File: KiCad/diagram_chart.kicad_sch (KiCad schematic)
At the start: 35 parts, among them J1 Barrel_Jack_Switch_Pin3Ring, J2 Screw_Terminal_01x02, SW0 SW_SPDT, U2 74HC165

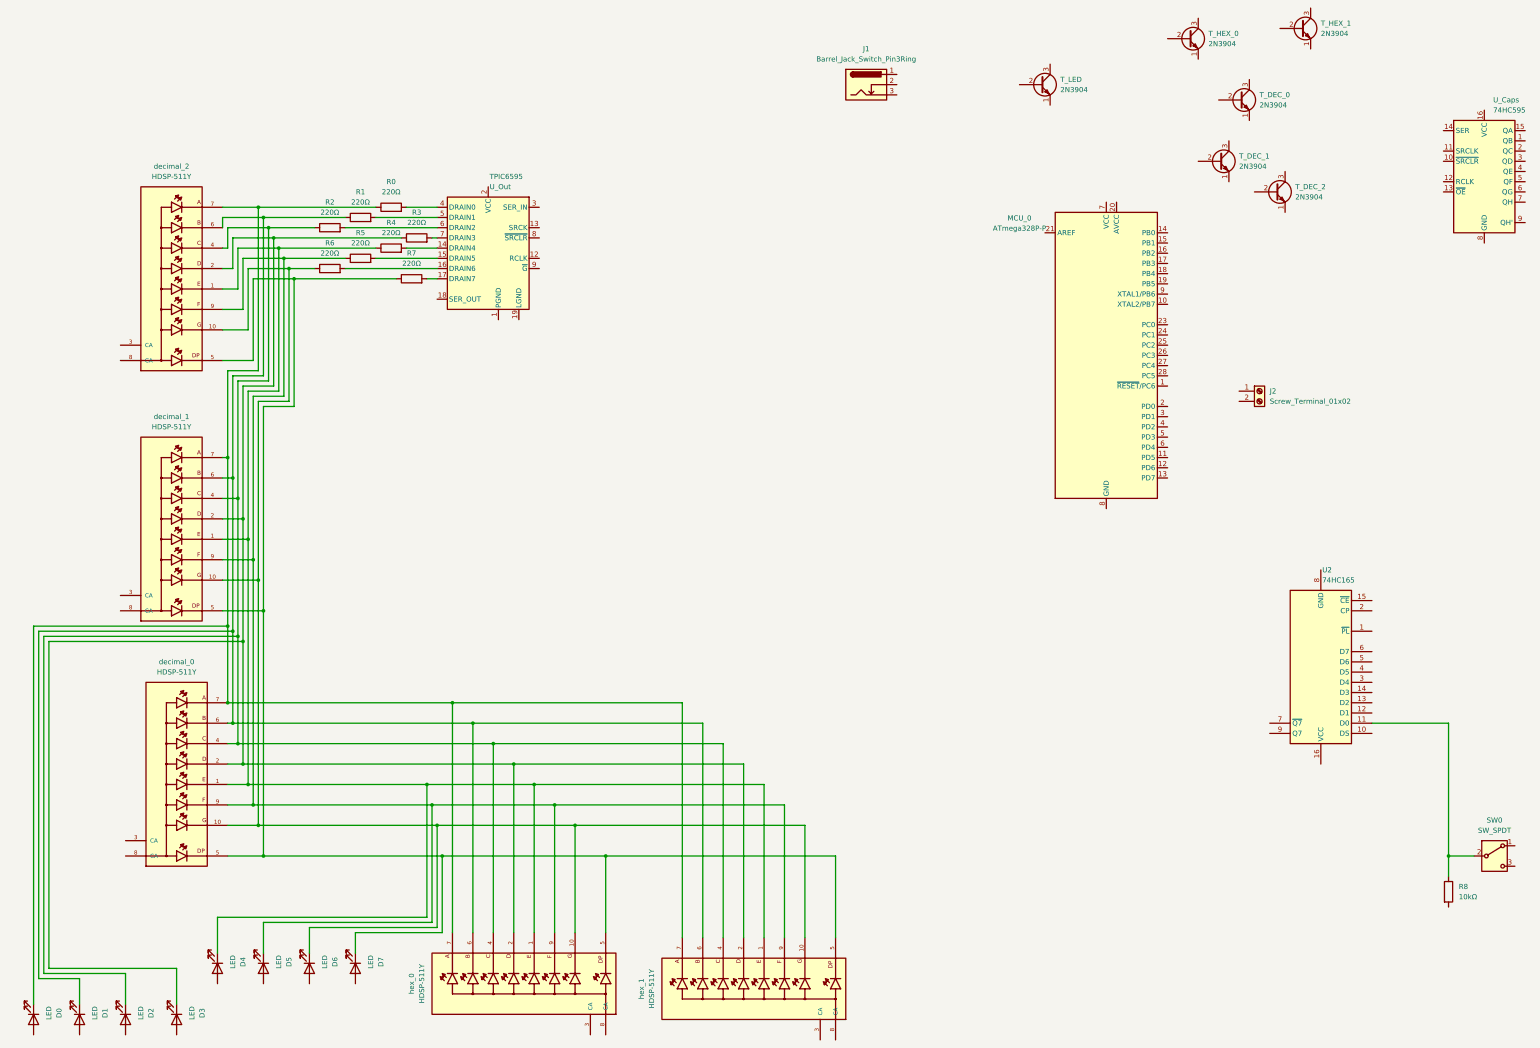
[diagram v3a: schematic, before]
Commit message: Connected all output-shift registers. Added Caps to ATMega Will need to fix the input-shift-register with switches. Also add Caps, then try to convert to PCB, then call night.
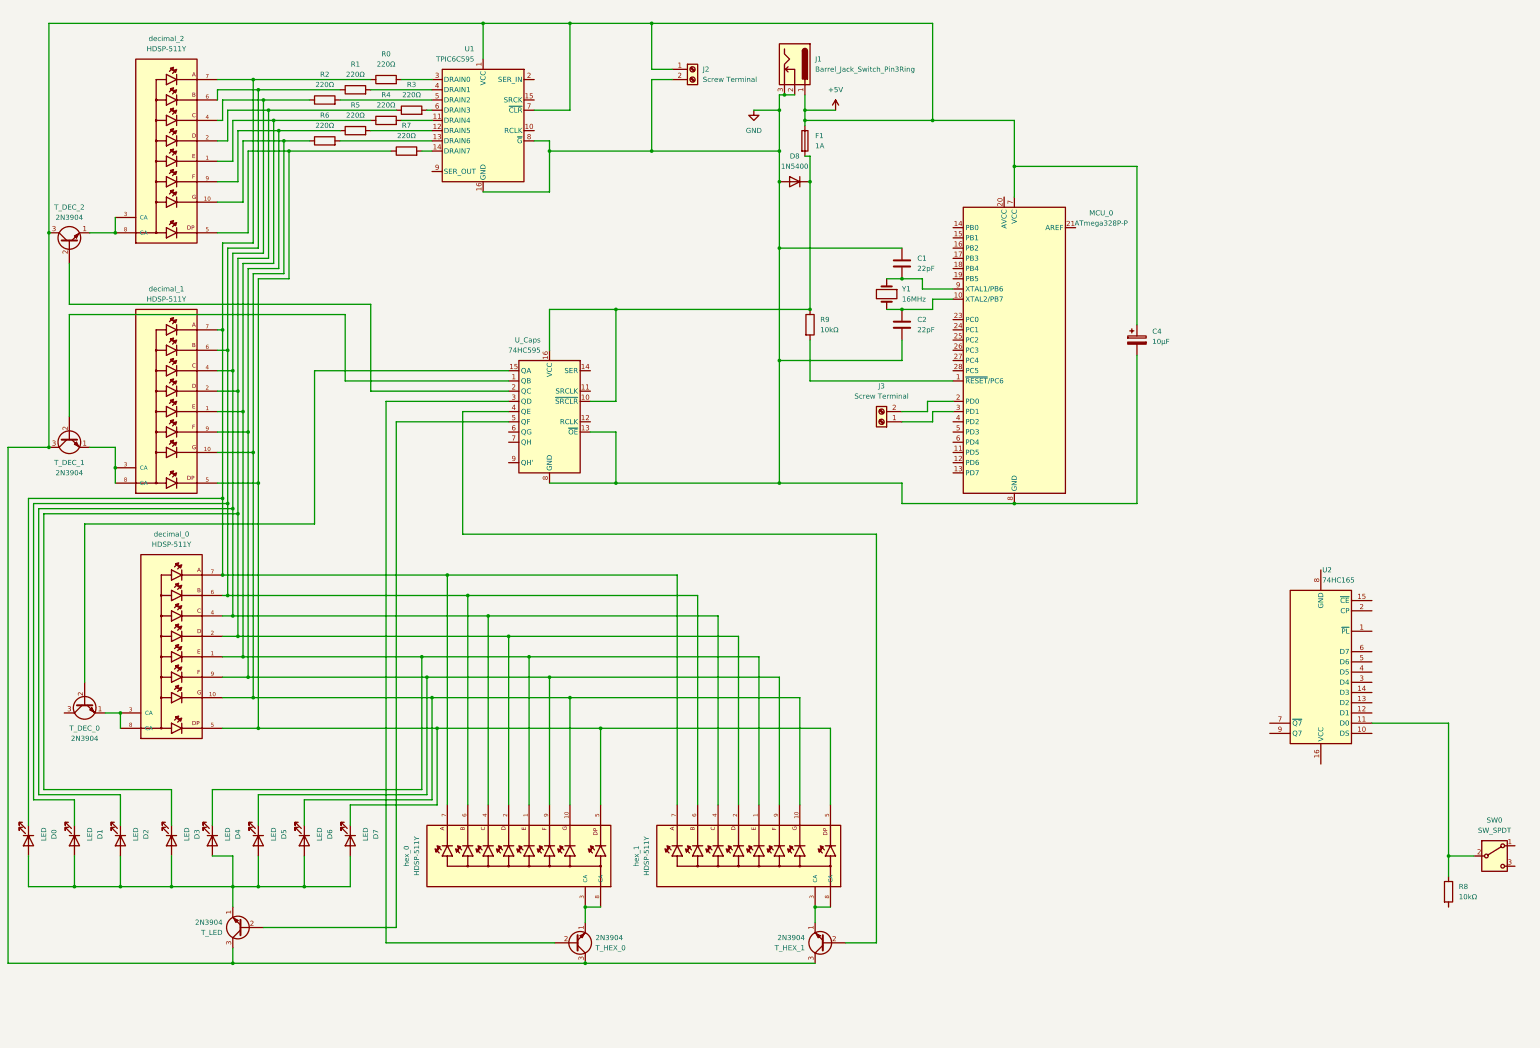
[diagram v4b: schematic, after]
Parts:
- removed U_Out: TPIC6595, Package_DIP:DIP-16_W7.62mm_Socket, symbol Interface_Expansion:TPIC6595
- added C1, C2: 22pF, Capacitor_THT:C_Disc_D3.0mm_W1.6mm_P2.50mm, symbol Device:C
- added C4: 10μF, Capacitor_THT:CP_Radial_D4.0mm_P2.00mm, symbol Device:C_Polarized
- added D8: 1N5400, Diode_THT:D_DO-201AD_P15.24mm_Horizontal, symbol Diode:1N5400
- added F1: 1A, Fuse:Fuseholder_Clip-5x20mm_Keystone_3512_Inline_P23.62x7.27mm_D1.02x1.57mm_Horizontal, symbol Device:Fuse
- added J3: Screw Terminal, TerminalBlock_Phoenix:TerminalBlock_Phoenix_MPT-0,5-2-2.54_1x02_P2.54mm_Horizontal, symbol Connector:Screw_Terminal_01x02
- added R9: 10kΩ, Resistor_THT:R_Axial_DIN0204_L3.6mm_D1.6mm_P5.08mm_Horizontal, symbol Device:R
- added U1: TPIC6C595, Package_DIP:DIP-16_W7.62mm_Socket, symbol TPIC6C595:TPIC6595
- added Y1: 16MHz, Crystal:Crystal_HC49-4H_Vertical, symbol Device:Crystal
- J2: value Screw_Terminal_01x02 -> Screw Terminal
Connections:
- net at R2.2: now also U1.5 (DRAIN2)
- net at hex_1.3 (CA): now also T_HEX_1.1 (E), hex_1.8 (CA)
- net at D4.2 (A): now also D0.2 (A), D1.2 (A), D2.2 (A), D3.2 (A), D5.2 (A), D6.2 (A), D7.2 (A), T_LED.1 (E)
- net at T_HEX_1.2 (B): now also U_Caps.4 (QE)
- net +5V: now reaches T_HEX_1.3 (C)
- net +5V: now also J1.1, J2.1 (Pin_1), MCU_0.7 (VCC), T_DEC_1.3 (C), T_DEC_2.3 (C), T_HEX_0.3 (C), T_LED.3 (C), C4.1, F1.1, U1.1 (VCC), U1.7 (~{CLR})
- net at T_LED.2 (B): now also U_Caps.5 (QF)
- net at R4.2: now also U1.11 (DRAIN4)
- net at U_Caps.1 (QB): now also T_DEC_1.2 (B)
- net at U_Caps.10 (~{SRCLR}): now also U_Caps.16 (VCC), D8.1 (K), F1.2, R9.1
- net GND: now reaches U_Caps.13 (~{OE})
- net GND: now also J1.2, J1.3, J2.2 (Pin_2), MCU_0.22 (GND), MCU_0.8 (GND), U_Caps.8 (GND), C1.1, C2.2, C4.2, D8.2 (A), U1.16 (GND), U1.8 (~{G})
- net at U_Caps.15 (QA): now also T_DEC_0.2 (B)
- net at U_Caps.2 (QC): now also T_DEC_2.2 (B)
- net at U_Caps.3 (QD): now also T_HEX_0.2 (B)
- net at decimal_0.3 (CA): now also T_DEC_0.1 (E), decimal_0.8 (CA)
- net at R6.2: now also U1.13 (DRAIN6)
- net at R1.2: now also U1.4 (DRAIN1)
- net at MCU_0.1 (~{RESET}/PC6): now also R9.2
- net at MCU_0.10 (XTAL2/PB7): now also C2.1, Y1.2
- net at MCU_0.2 (PD0): now also J3.2 (Pin_2)
- net at MCU_0.3 (PD1): now also J3.1 (Pin_1)
- net at MCU_0.9 (XTAL1/PB6): now also C1.2, Y1.1
- net at R7.2: now also U1.14 (DRAIN7)
- net at T_HEX_0.1 (E): now also hex_0.3 (CA), hex_0.8 (CA)
- net at decimal_1.3 (CA): now also T_DEC_1.1 (E), decimal_1.8 (CA)
- net at R3.2: now also U1.6 (DRAIN3)
- net at R0.2: now also U1.3 (DRAIN0)
- net at R5.2: now also U1.12 (DRAIN5)
- net at T_DEC_2.1 (E): now also decimal_2.3 (CA), decimal_2.8 (CA)
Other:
- moved on the sheet: D0, D1, D2, D3, D4, D5, D6, D7, J1, J2, MCU_0, R0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

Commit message: Added a lot of caps and wires Will try to convert to PCB Will tomorrow need to verrify
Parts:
- added CU1, CU_Caps: 100nF, Capacitor_THT:C_Disc_D3.0mm_W1.6mm_P2.50mm, symbol Device:C
- added R10, R11, R12, R13, R14, R15, R16, R17, R22: 10kΩ, Resistor_THT:R_Axial_DIN0204_L3.6mm_D1.6mm_P5.08mm_Horizontal, symbol Device:R
- added R18, R19, R20, R21: 0Ω, Resistor_THT:R_Axial_DIN0204_L3.6mm_D1.6mm_P2.54mm_Vertical, symbol Device:R
- added R23, R24, R25, R26, R27, R28: 1KΩ, Resistor_THT:R_Axial_DIN0207_L6.3mm_D2.5mm_P7.62mm_Horizontal, symbol Device:R
- added RGB: Screw Terminal, TerminalBlock_Phoenix:TerminalBlock_Phoenix_MPT-0,5-2-2.54_1x02_P2.54mm_Horizontal, symbol Connector:Screw_Terminal_01x02
- added SW1, SW2, SW3, SW4, SW5, SW6, SW7: SW_SPDT, switch:SW_Toggle_Blue_wSlots, symbol Switch:SW_SPDT
- added SW_N: NXT_BTN, Button_Switch_THT:SW_PUSH_6mm_H5mm, symbol Switch:SW_Push
- renumbered C4 to C_MCU
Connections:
- net +5V: no longer C_MCU.1, J2.1 (Pin_1), MCU_0.7 (VCC), T_DEC_1.3 (C), T_DEC_2.3 (C), T_HEX_0.3 (C), T_HEX_1.3 (C), T_LED.3 (C), U1.1 (VCC), U1.7 (~{CLR})
- net GND: now also R8.2, SW0.1 (A), U2.15 (~{CE}), U2.8 (GND), CU1.2, CU_Caps.2, R10.2, R11.2, R12.2, R13.2, R14.2, R15.2, R16.2, R17.2, R18.2, SW1.1 (A), SW2.1 (A), SW3.1 (A), SW4.1 (A), SW5.1 (A), SW6.1 (A), SW7.1 (A); no longer U_Caps.13 (~{OE})
- net at SW0.3 (C): now also C_MCU.1, D8.1 (K), F1.2, J2.1 (Pin_1), MCU_0.7 (VCC), R9.1, T_DEC_0.3 (C), T_DEC_1.3 (C), T_DEC_2.3 (C), T_HEX_0.3 (C), T_HEX_1.3 (C), T_LED.3 (C), U1.1 (VCC), U2.16 (VCC), U_Caps.10 (~{SRCLR}), U_Caps.16 (VCC), CU1.1, CU_Caps.1, R22.1, SW1.3 (C), SW2.3 (C), SW3.3 (C), SW4.3 (C), SW5.3 (C), SW6.3 (C), SW7.3 (C), SW_N.2
- net at U2.1 (~{PL}): now also MCU_0.13 (PD7)
- net at U2.12 (D1): now also R11.1, SW1.2 (B)
- net at U2.13 (D2): now also R12.1, SW2.2 (B)
- net at U2.14 (D3): now also R13.1, SW3.2 (B)
- net at U2.2 (CP): now also MCU_0.12 (PD6), U1.15 (SRCK), U_Caps.11 (SRCLK)
- net at U2.3 (D4): now also R14.1, SW4.2 (B)
- net at U2.4 (D5): now also R15.1, SW5.2 (B)
- net at U2.5 (D6): now also R16.1, SW6.2 (B)
- net at U2.6 (D7): now also R17.1, SW7.2 (B)
- net at U2.9 (Q7): now also R20.1, R21.2
- net at T_HEX_1.2 (B): now also R25.1; no longer U_Caps.4 (QE)
- net at T_LED.2 (B): now also R23.1; no longer U_Caps.5 (QF)
- net at U_Caps.1 (QB): now also R27.2; no longer T_DEC_1.2 (B)
- net at U_Caps.12 (RCLK): now also MCU_0.15 (PB1)
- net at U_Caps.14 (SER): now also MCU_0.6 (PD4), U1.2 (SER_IN), R20.2
- net at U_Caps.15 (QA): now also R26.2; no longer T_DEC_0.2 (B)
- net at U_Caps.2 (QC): now also R28.1; no longer T_DEC_2.2 (B)
- net at U_Caps.3 (QD): now also R24.1; no longer T_HEX_0.2 (B)
- net at MCU_0.11 (PD5): now also R21.1
- net at MCU_0.14 (PB0): now also U1.10 (RCLK)
- net at MCU_0.16 (PB2): now also RGB.1 (Pin_1)
- net at MCU_0.4 (PD2): now also R19.2
- net at MCU_0.5 (PD3): now also R10.1, SW_N.1
- new net: R18.1, R19.1, U_Caps.13 (~{OE})
- new net: R25.2, U_Caps.4 (QE)
- new net: R23.2, U_Caps.5 (QF)
- new net: R24.2, T_HEX_0.2 (B)
- new net: R28.2, T_DEC_2.2 (B)
- new net: R22.2, U1.7 (~{CLR})
- new net: R26.1, T_DEC_0.2 (B)
- new net: R27.1, T_DEC_1.2 (B)
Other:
- moved on the sheet: J3

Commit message: Added NC flags, will now annote everything
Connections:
- net at CU1.1, CU_Caps.1, C_MCU.1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: now also MCU_0.20 (AVCC)
- no-connect marks 0 -> 16
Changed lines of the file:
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@@
   (junction (at 86.36 48.26) (diameter 0) (color 0 0 0 0)
   )
+  (junction (at 266.7 59.69) (diameter 0) (color 0 0 0 0)
+  )
   (junction (at 71.12 135.89) (diameter 0) (color 0 0 0 0)
   )
@@
   (junction (at 405.13 210.82) (diameter 0.2) (color 0 0 0 1)
   )
+  (no_connect (at 140.97 120.65))
+  (no_connect (at 251.46 74.93))
+  (no_connect (at 251.46 97.79))
+  (no_connect (at 251.46 95.25))
+  (no_connect (at 330.2 190.5))
+  (no_connect (at 251.46 77.47))
+  (no_connect (at 251.46 92.71))
+  (no_connect (at 251.46 102.87))
+  (no_connect (at 251.46 90.17))
+  (no_connect (at 355.6 193.04))
+  (no_connect (at 140.97 125.73))
+  (no_connect (at 248.92 60.96))
+  (no_connect (at 121.92 53.34))
+  (no_connect (at 140.97 118.11))
+  (no_connect (at 251.46 100.33))
+  (no_connect (at 251.46 80.01))
   (wire (pts (xy 373.38 176.53) (xy 363.22 176.53))
     (stroke (width 0) (type default))
@@
     (stroke (width 0) (type default))
   )
+  (wire (pts (xy 264.16 59.69) (xy 266.7 59.69))
+    (stroke (width 0.2) (type default) (color 255 0 0 1))
+  )
   (wire (pts (xy 251.46 82.55) (xy 243.84 82.55))

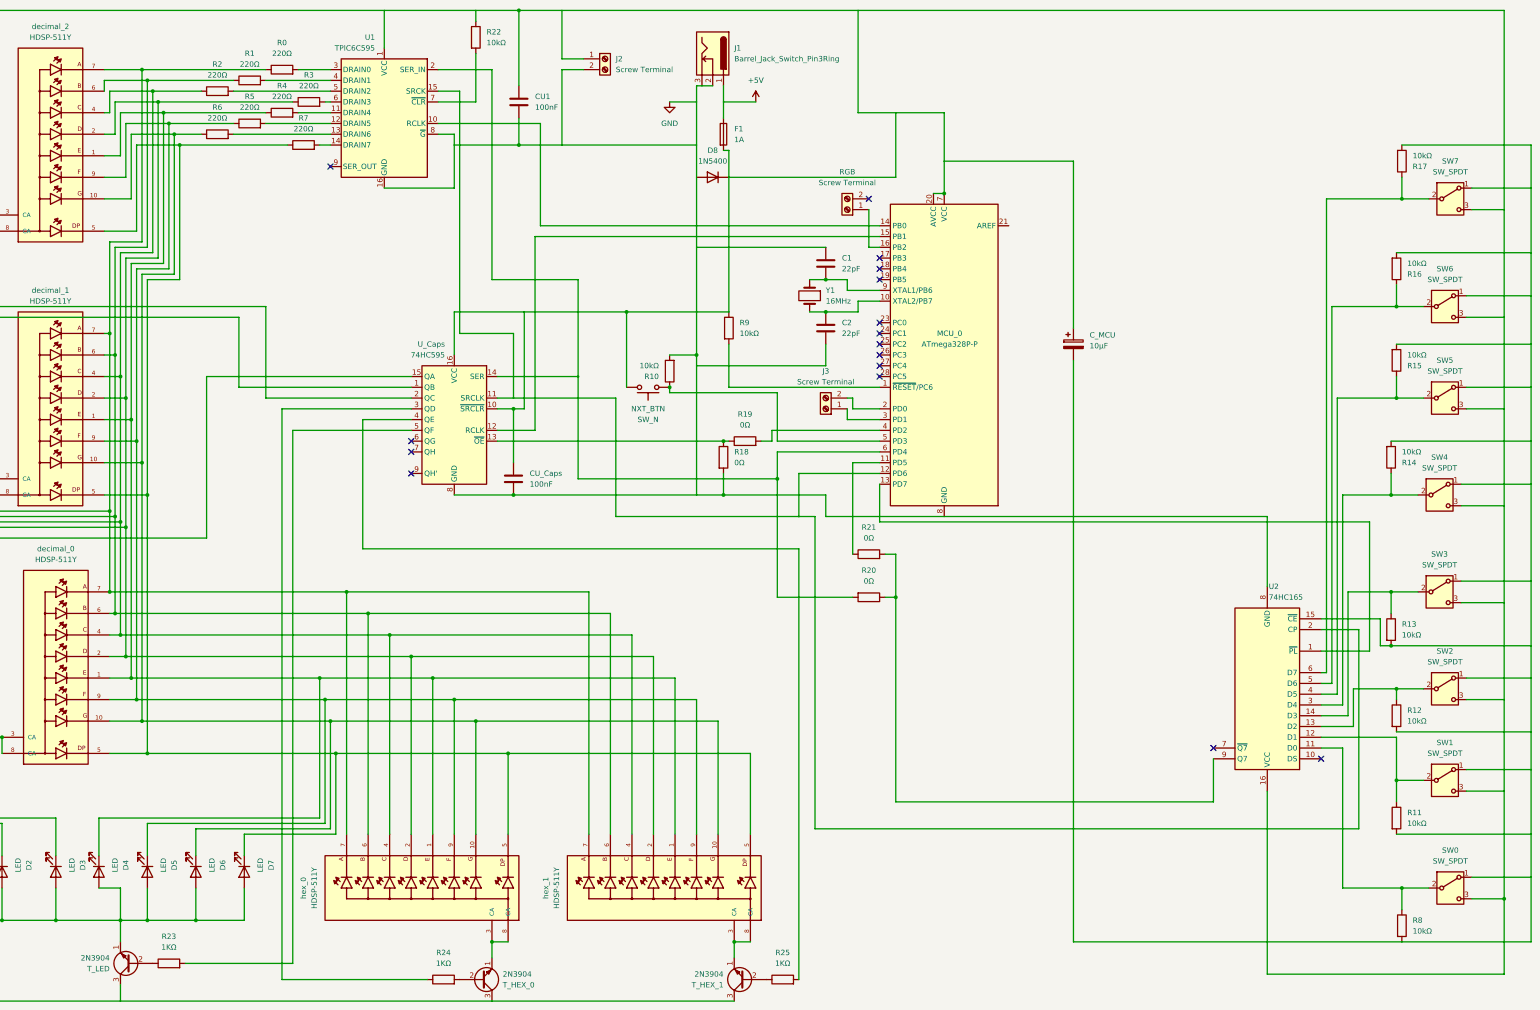
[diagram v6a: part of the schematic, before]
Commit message: Created PCB. Will need to map traces, and sizes tomorrow. Maybe order tomorrow or more probably tuesday next week.
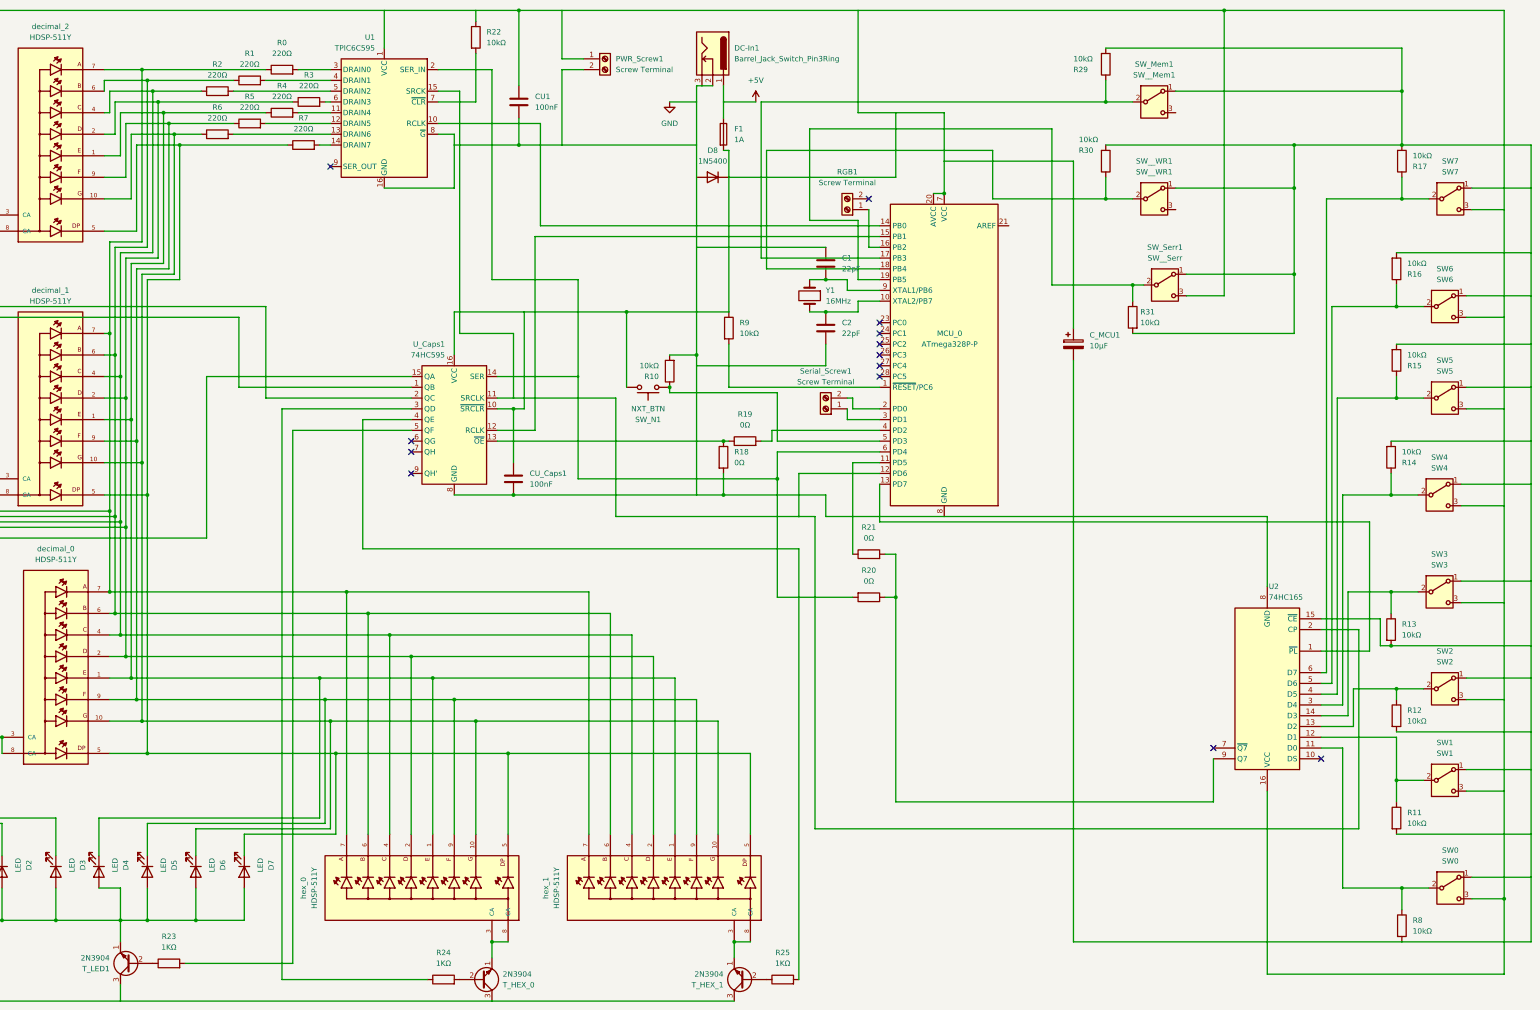
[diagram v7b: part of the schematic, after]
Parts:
- added R29, R30, R31: 10kΩ, Resistor_THT:R_Axial_DIN0204_L3.6mm_D1.6mm_P5.08mm_Horizontal, symbol Device:R
- added SW_Mem1: SW__Mem1, switch:SW_Toggle_Blue_wSlots, symbol Switch:SW_SPDT
- added SW_Serr1: SW__Serr, switch:SW_Toggle_Blue_wSlots, symbol Switch:SW_SPDT
- added SW__WR1: SW__WR1, switch:SW_Toggle_Blue_wSlots, symbol Switch:SW_SPDT
- SW0: value SW_SPDT -> SW0
- SW1: value SW_SPDT -> SW1
- SW2: value SW_SPDT -> SW2
- SW3: value SW_SPDT -> SW3
- SW4: value SW_SPDT -> SW4
- SW5: value SW_SPDT -> SW5
- SW6: value SW_SPDT -> SW6
- SW7: value SW_SPDT -> SW7
- renumbered CU_Caps to CU_Caps1, C_MCU to C_MCU1, J1 to DC-In1, J2 to PWR_Screw1, RGB to RGB1, SW_N to SW_N1, J3 to Serial_Screw1, T_LED to T_LED1, U_Caps to U_Caps1
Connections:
- net GND: now also R29.2, R30.2, R31.2, SW_Mem1.1 (A), SW_Serr1.1 (A), SW__WR1.1 (A)
- net at CU1.1, CU_Caps1.1, C_MCU1.1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: now also SW_Serr1.3 (C)
- net at MCU_0.17 (PB3): now also R29.1, SW_Mem1.2 (B)
- net at MCU_0.18 (PB4): now also R30.1, SW__WR1.2 (B)
- net at MCU_0.19 (PB5): now also R31.1, SW_Serr1.2 (B)
- no-connect marks 16 -> 13
